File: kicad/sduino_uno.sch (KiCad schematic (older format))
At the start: 45 parts, among them J1 Conn_01x04, J2 Conn_01x02, Q1 FDN340P, U1 NCP1117-5.0_SOT223, U2 NCP1117-3.3_SOT223, U3 CH340G, U4 STM8S105K_LQFP32, U5 LM358, U6 STM8S105K_UFQFPN32, X1 Jack-DC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

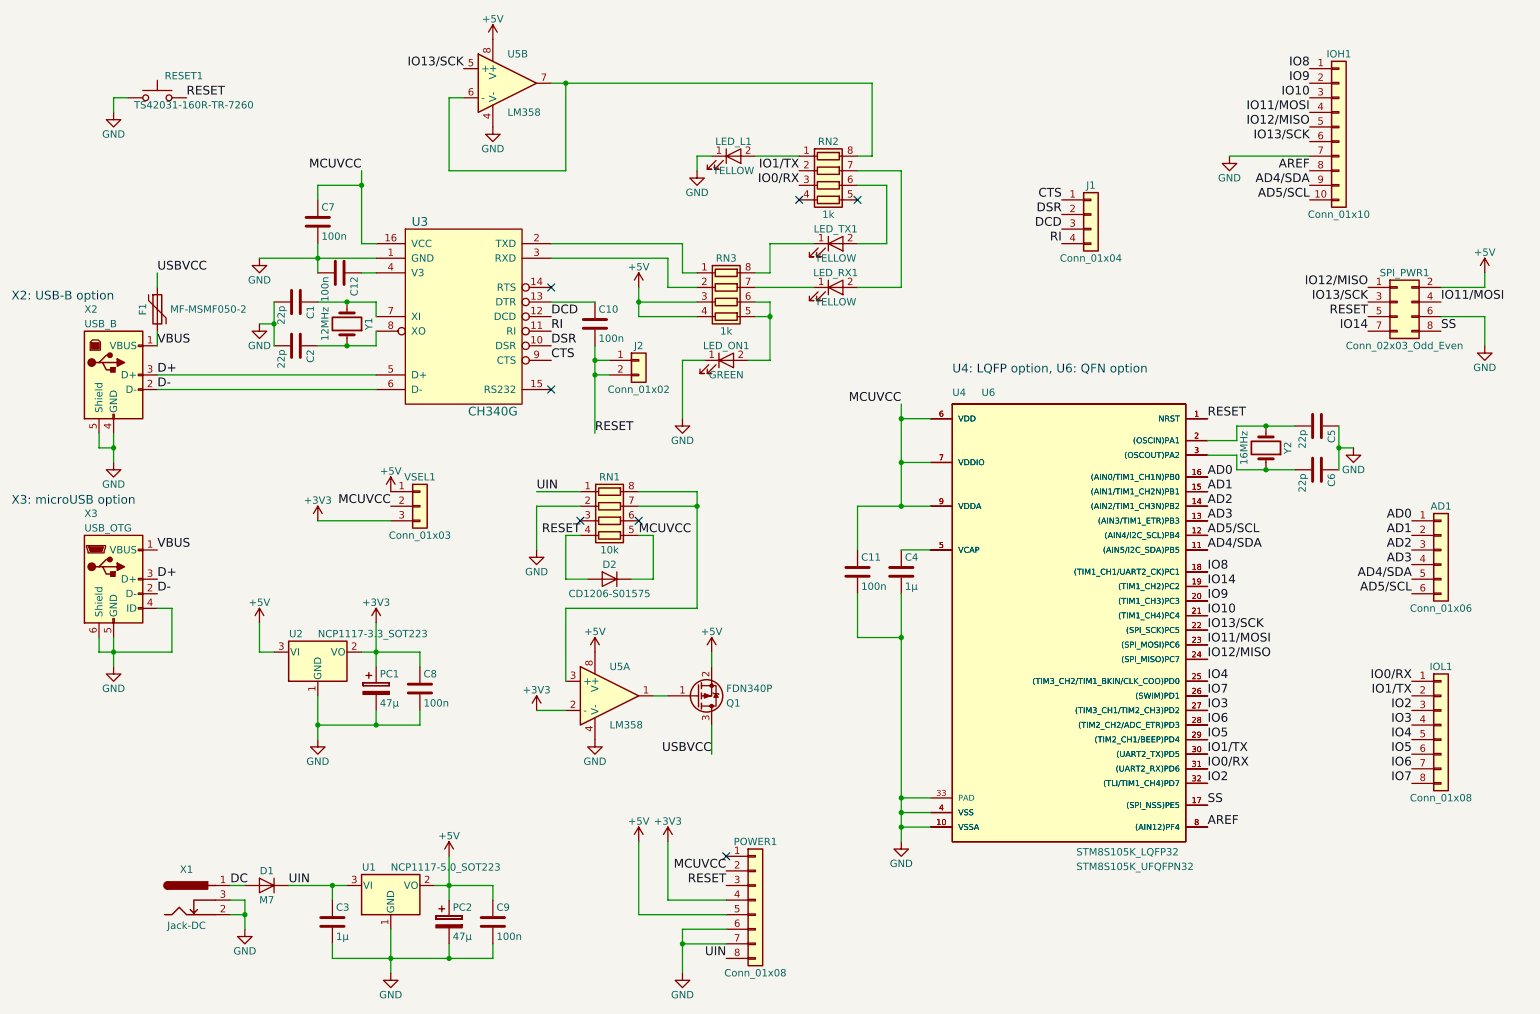
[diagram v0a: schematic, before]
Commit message: revision 2017-10-08 - fix major error in TX/RX wiring (LEDs were connected in series) - improve ground fill surrounding crystals - rename IO14 to IO23 - add some pin numbers on the back side - update documentation
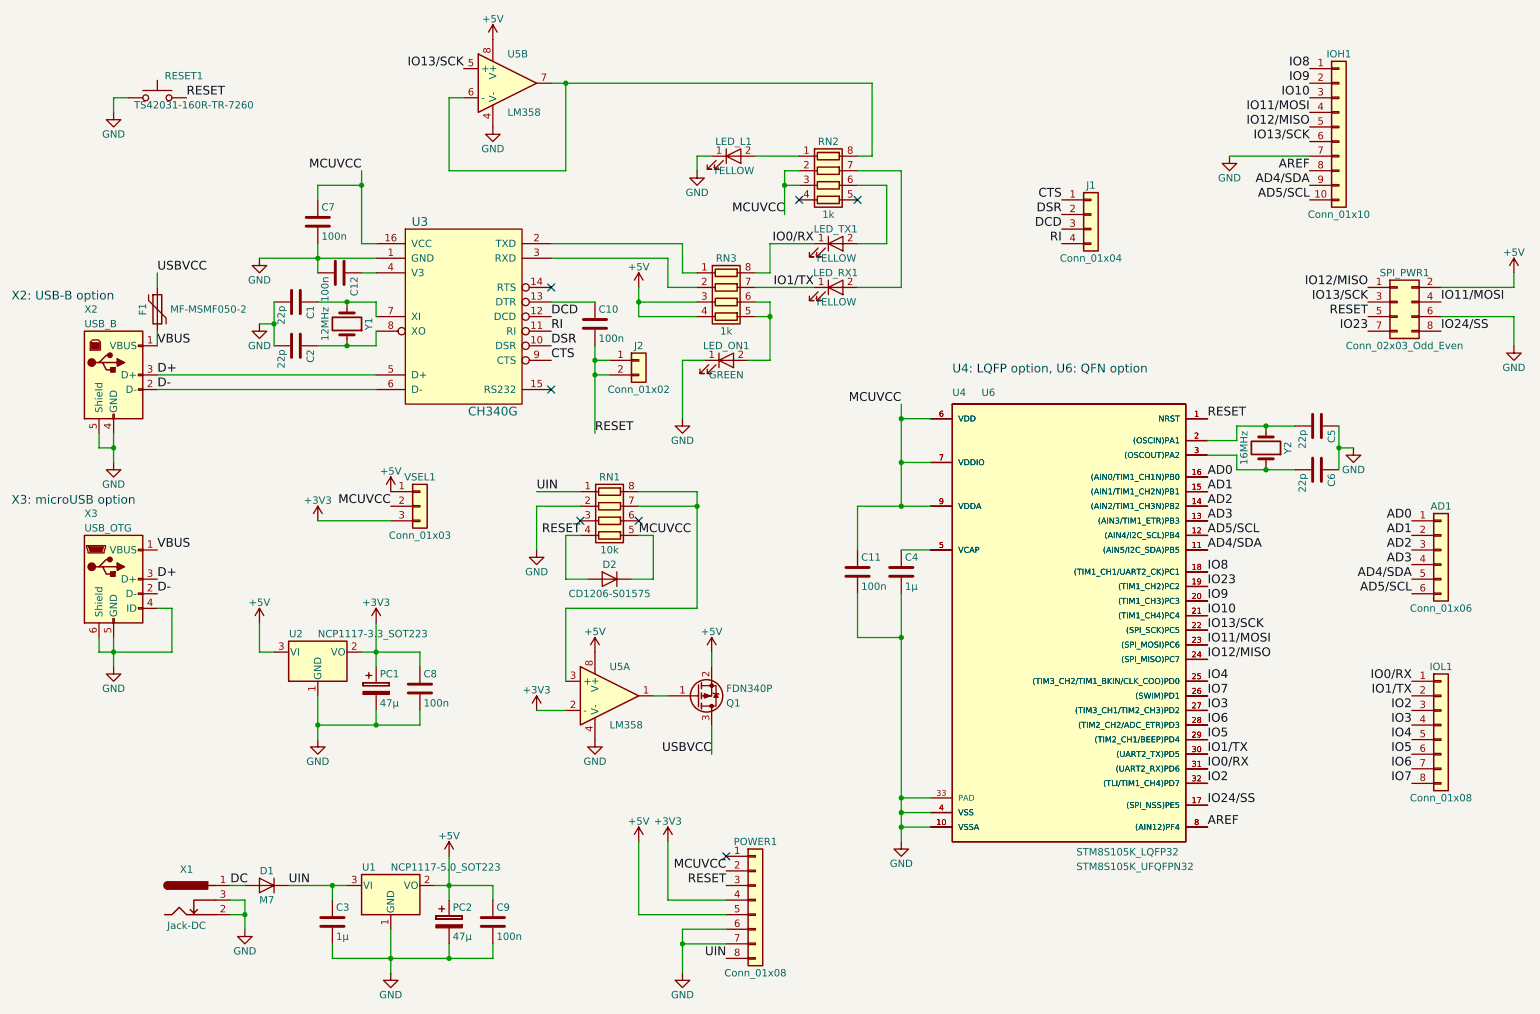
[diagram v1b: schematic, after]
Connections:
- net IO0/RX: now also LED_TX1.1 (K), RN3.8 (R1.2); no longer RN2.3 (R3.1)
- net IO1/TX: now also LED_RX1.1 (K), RN3.7 (R2.2); no longer RN2.2 (R2.1)
- net MCUVCC: now also RN2.2 (R2.1), RN2.3 (R3.1)
- net IO14 renamed IO23
- net SS renamed IO24/SS
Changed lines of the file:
@@
 Title "sduino UNO"
 Date "2017-09-15"
-Rev "2017-10-01"
-Comp ""
-Comment1 ""
-Comment2 ""
-Comment3 ""
-Comment4 ""
+Rev "2017-10-08"
+Comp "Benedikt Freisen"
+Comment1 "see http://creativecommons.org/licenses/by-sa/2.5/"
+Comment2 "Released under Creative Commons Attribution-ShareAlike 2.5 Generic License,"
+Comment3 "In part based on Arduino UNO design, see arduino.cc"
+Comment4 "A development board with STM8S105K6 MCU in Arduino UNO form factor"
 $EndDescr
 $Comp
@@
 IO10
 Text Label 8800 6050 0    60   ~ 0
-SS
+IO24/SS
 Text Label 8800 4550 0    60   ~ 0
-IO14
+IO23
 Text Label 10200 4100 2    60   ~ 0
 AD0
@@
 L GND #PWR020
 U 1 1 59BEB375
-P 10700 2900
-F 0 "#PWR020" H 10700 2650 50  0001 C CNN
-F 1 "GND" H 10700 2750 50  0000 C CNN
-F 2 "" H 10700 2900 50  0001 C CNN
-F 3 "" H 10700 2900 50  0001 C CNN
-	1    10700 2900
+P 10900 2900
+F 0 "#PWR020" H 10900 2650 50  0001 C CNN
+F 1 "GND" H 10900 2750 50  0000 C CNN
+F 2 "" H 10900 2900 50  0001 C CNN
+F 3 "" H 10900 2900 50  0001 C CNN
+	1    10900 2900
 	1    0    0    -1
 $EndComp
@@
 	1    0    0    -1
 $EndComp
-Text Label 6000 1800 2    60   ~ 0
+Text Label 6100 2200 2    60   ~ 0
 IO0/RX
-Text Label 6000 1700 2    60   ~ 0
+Text Label 6100 2500 2    60   ~ 0
 IO1/TX
 Text Label 4500 4200 2    60   ~ 0
@@
 USBVCC
 Text Label 9900 2800 2    60   ~ 0
-IO14
+IO23
 Text Label 10400 2800 0    60   ~ 0
-SS
+IO24/SS
 $Comp
 L +5V #PWR029
 U 1 1 59BF0D38
-P 10700 2400
-F 0 "#PWR029" H 10700 2250 50  0001 C CNN
-F 1 "+5V" H 10700 2540 50  0000 C CNN
-F 2 "" H 10700 2400 50  0001 C CNN
-F 3 "" H 10700 2400 50  0001 C CNN
-	1    10700 2400
+P 10900 2400
+F 0 "#PWR029" H 10900 2250 50  0001 C CNN
+F 1 "+5V" H 10900 2540 50  0000 C CNN
+F 2 "" H 10900 2400 50  0001 C CNN
+F 3 "" H 10900 2400 50  0001 C CNN
+	1    10900 2400
 	1    0    0    -1
 $EndComp
@@
 	5000 5300 5100 5300
 Wire Wire Line
-	10400 2700 10700 2700
-Wire Wire Line
-	10700 2700 10700 2900
-Wire Wire Line
-	10400 2500 10700 2500
-Wire Wire Line
-	10700 2500 10700 2400
+	10400 2700 10900 2700
+Wire Wire Line
+	10400 2500 10900 2500
 Wire Wire Line
 	1300 1300 1300 1200
@@
 	6900 6000 6700 6000
 Connection ~ 6700 6000
+Text Label 5900 2000 2    60   ~ 0
+MCUVCC
+Wire Wire Line
+	6000 1700 5900 1700
+Wire Wire Line
+	5900 1700 5900 2000
+Wire Wire Line
+	6000 1800 5900 1800
+Connection ~ 5900 1800
+Wire Wire Line
+	10900 2500 10900 2400
+Wire Wire Line
+	10900 2700 10900 2900
 $EndSCHEMATC

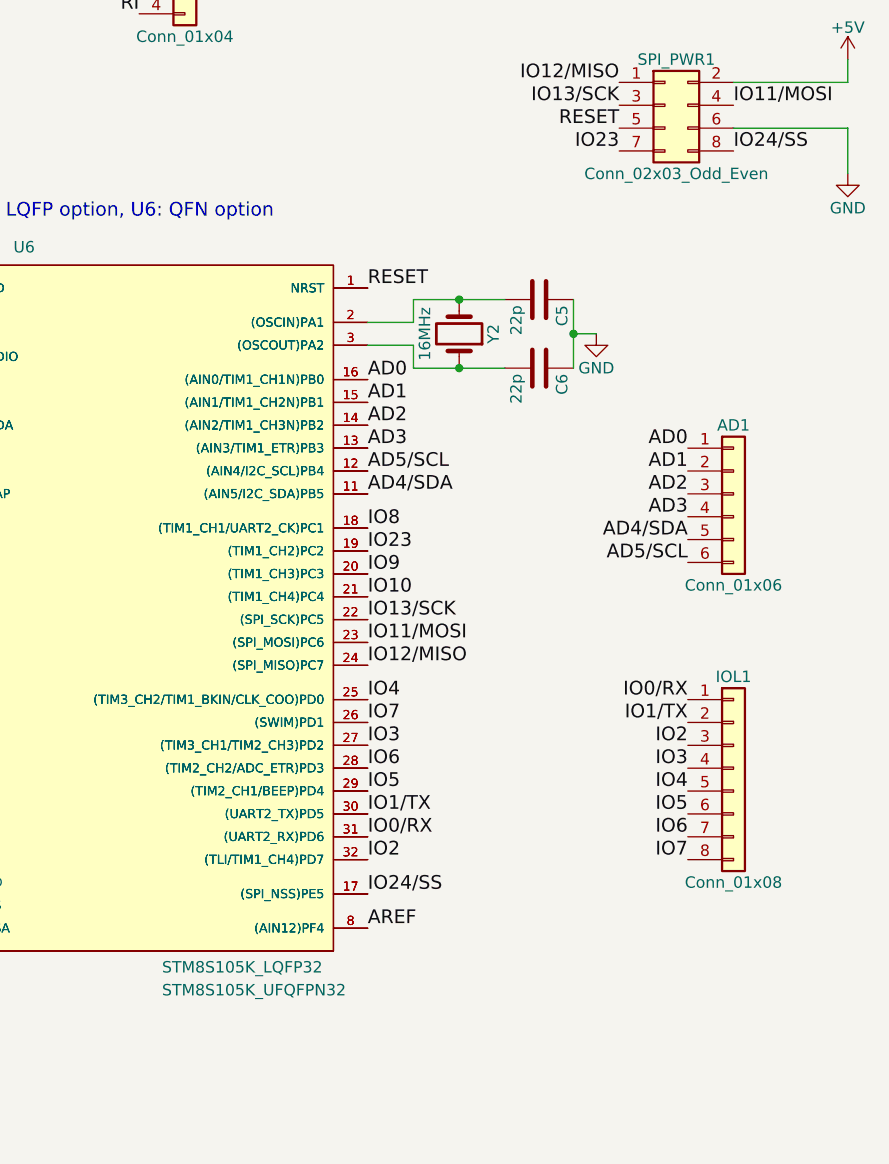
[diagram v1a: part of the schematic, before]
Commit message: board revision 2017-11-15 (minor corrections and clarifications)
- use more precise names for some components
- adjust footprint of DC jack to better fit the DC jack
- adjust thermal relief around pads of 0603 components
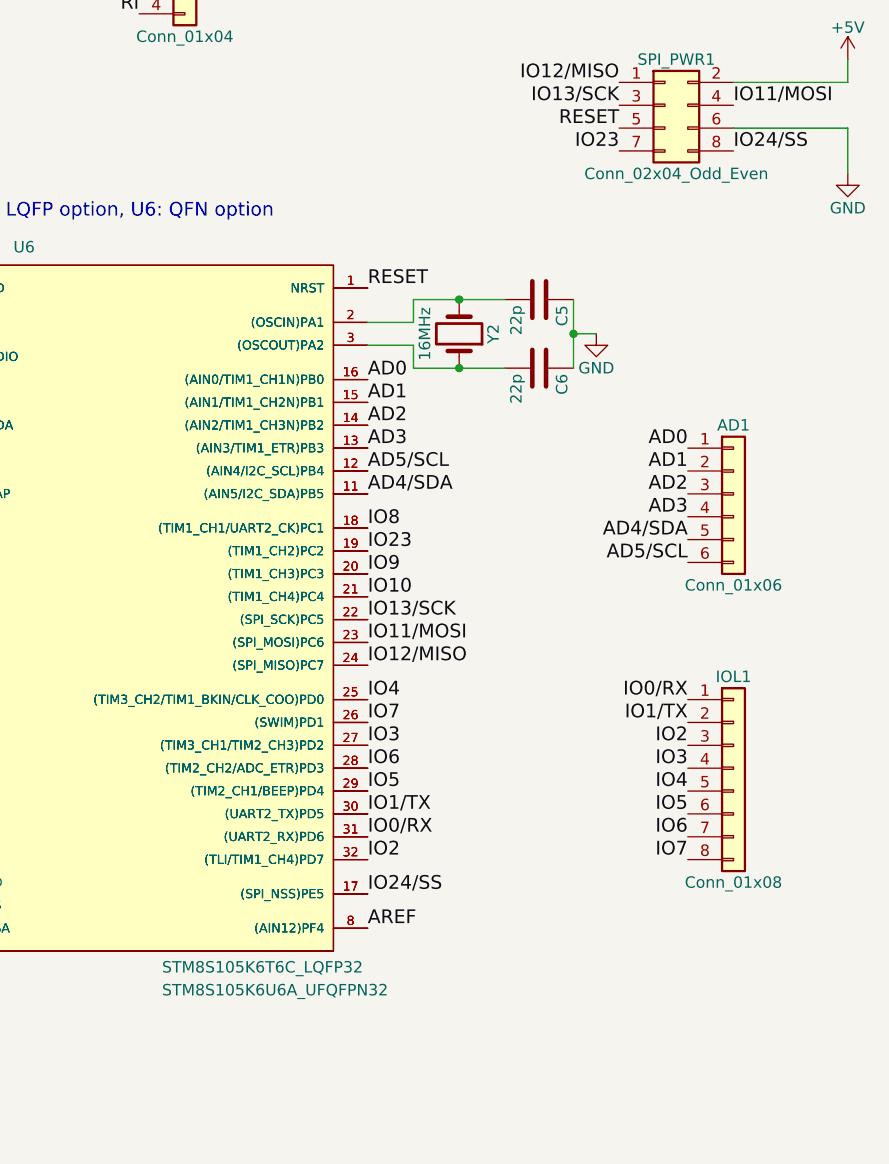
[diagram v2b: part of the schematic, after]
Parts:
- SPI_PWR1: value Conn_02x03_Odd_Even -> Conn_02x04_Odd_Even
- U4: value STM8S105K_LQFP32 -> STM8S105K6T6C_LQFP32
- U6: value STM8S105K_UFQFPN32 -> STM8S105K6U6A_UFQFPN32
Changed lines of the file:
@@
 Title "sduino UNO"
 Date "2017-09-15"
-Rev "2017-10-08"
+Rev "2017-11-15"
 Comp "Benedikt Freisen"
 Comment1 "see http://creativecommons.org/licenses/by-sa/2.5/"
@@
 P 10100 2600
 F 0 "SPI_PWR1" H 10150 2800 50  0000 C CNN
-F 1 "Conn_02x03_Odd_Even" H 10150 2300 50  0000 C CNN
+F 1 "Conn_02x04_Odd_Even" H 10150 2300 50  0000 C CNN
 F 2 "Pin_Headers:Pin_Header_Straight_2x04_Pitch2.54mm" H 10100 2600 50  0001 C CNN
 F 3 "" H 10100 2600 50  0001 C CNN
@@
 P 7850 4800
 F 0 "U4" H 7050 6350 50  0000 L BNN
-F 1 "STM8S105K_LQFP32" H 7900 3200 50  0000 L BNN
+F 1 "STM8S105K6T6C_LQFP32" H 7900 3200 50  0000 L BNN
 F 2 "Housings_QFP:LQFP-32_7x7mm_Pitch0.8mm" H 7850 3750 60  0001 C CNN
 F 3 "" H 7850 3750 60  0001 C CNN
@@
 P 7850 4800
 F 0 "U6" H 7250 6350 50  0000 L BNN
-F 1 "STM8S105K_UFQFPN32" H 7900 3100 50  0000 L BNN
+F 1 "STM8S105K6U6A_UFQFPN32" H 7900 3100 50  0000 L BNN
 F 2 "Housings_DFN_QFN:QFN-32-1EP_5x5mm_Pitch0.5mm" H 7850 3750 60  0001 C CNN
 F 3 "" H 7850 3750 60  0001 C CNN
